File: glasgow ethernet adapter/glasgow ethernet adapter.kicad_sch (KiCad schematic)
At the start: 25 parts, among them J1 RJ45_Shielded, J2 Conn_02x10_Counter_Clockwise_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, J3 Conn_02x10_Counter_Clockwise_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, Y1 25MHz

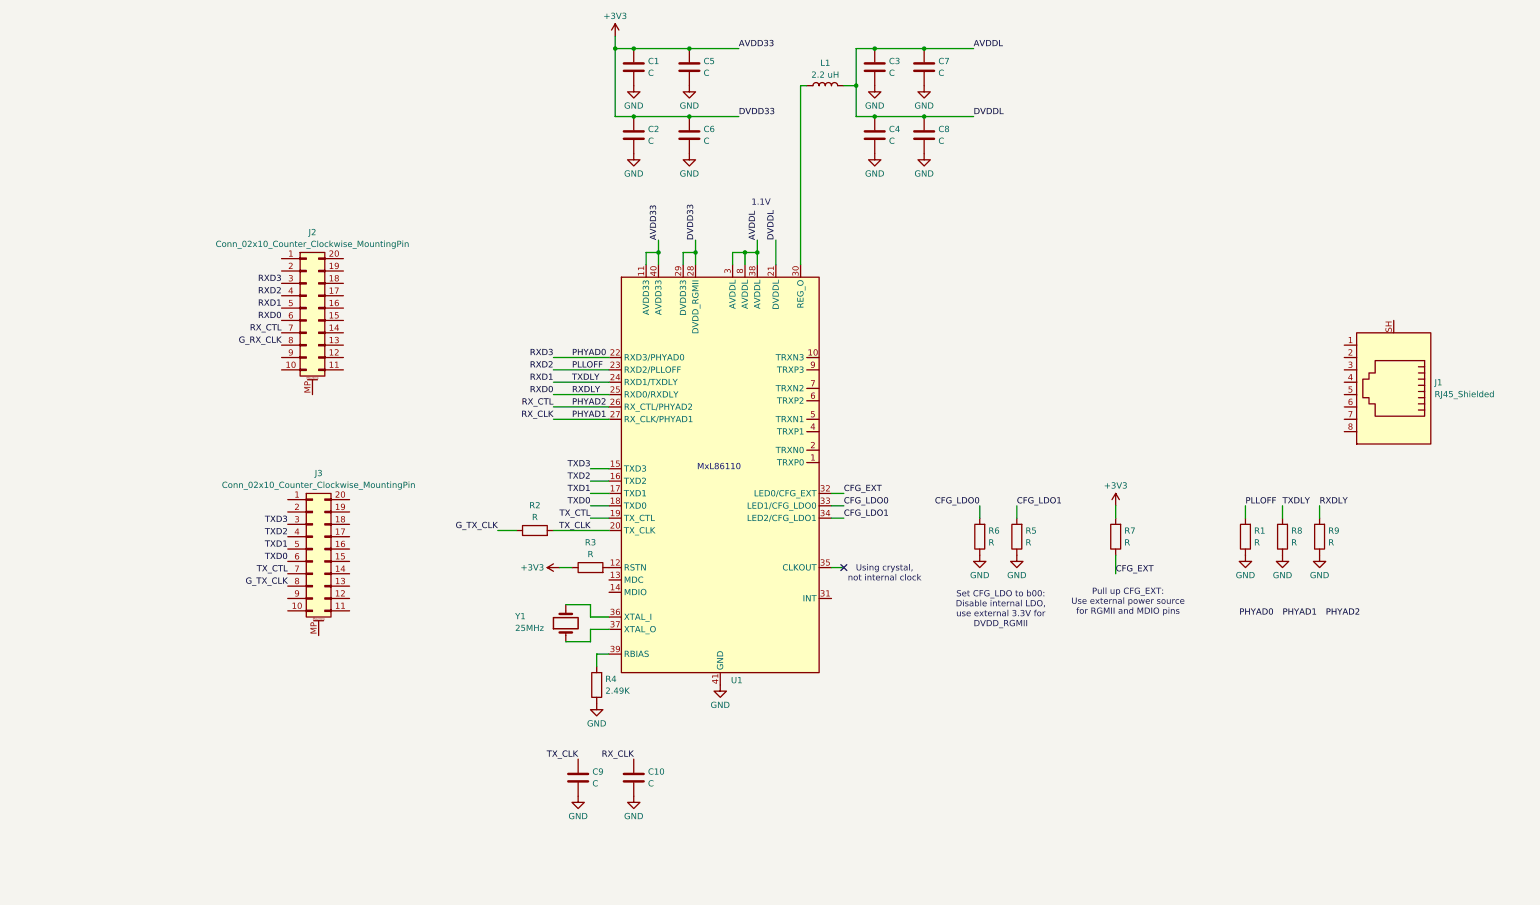
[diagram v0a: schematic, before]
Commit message: add transformer + protoype layout for transformer
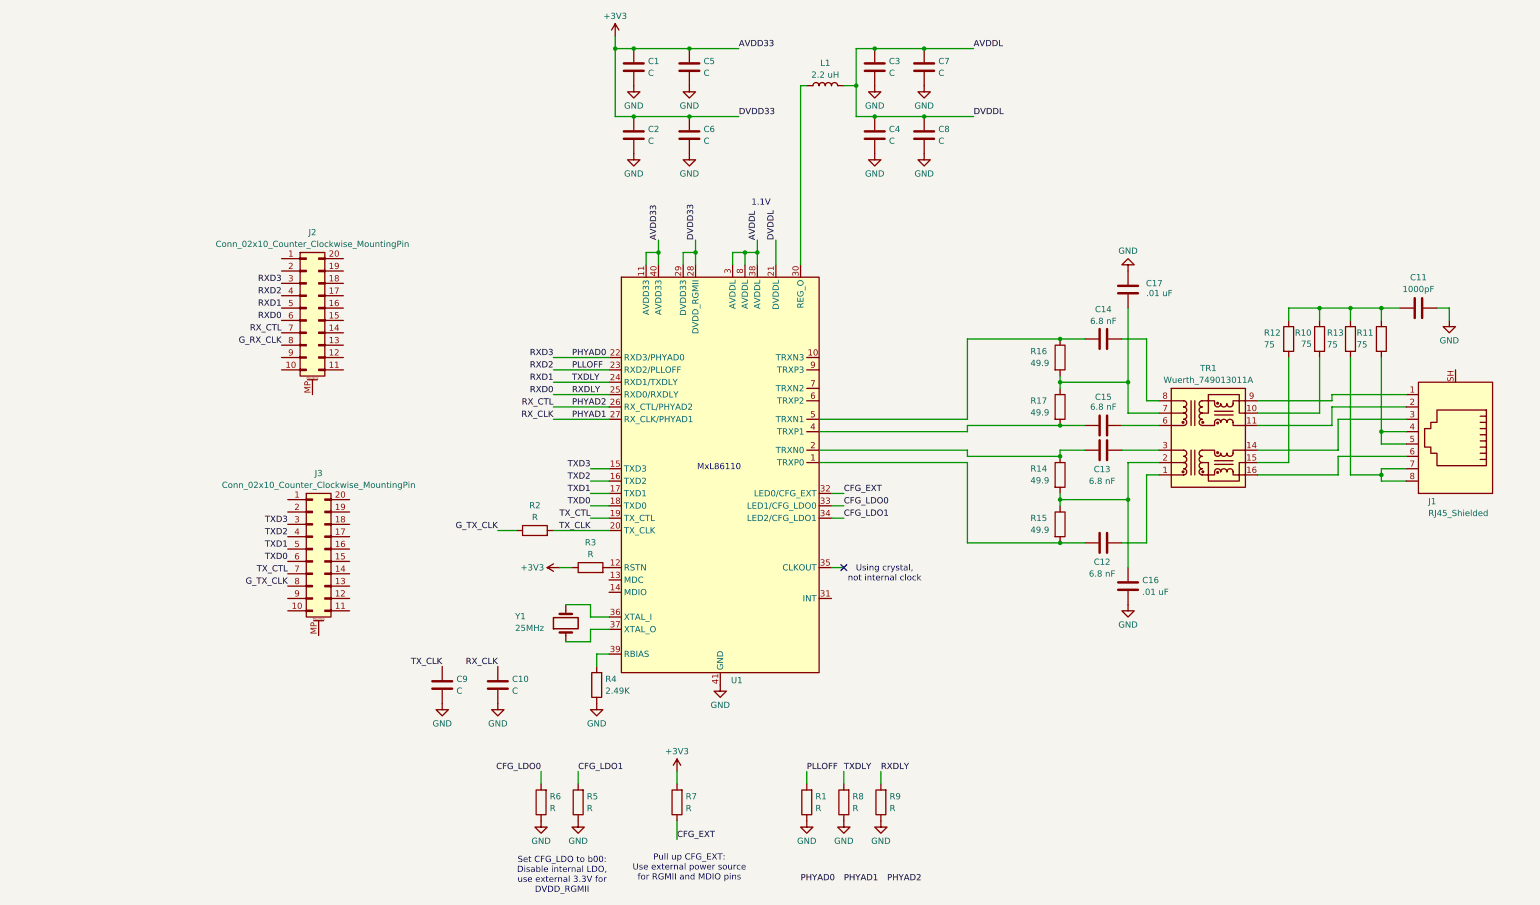
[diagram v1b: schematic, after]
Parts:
- added C11: 1000pF, symbol Device:C
- added C12, C13, C14, C15: 6.8 nF, symbol Device:C
- added C16, C17: .01 uF, symbol Device:C
- added R10, R11, R12, R13: 75, symbol Device:R
- added R14, R15, R16, R17: 49.9, symbol Device:R
- added TR1: Wuerth_749013011A, Transformer_SMD:Transformer_Ethernet_Wuerth_749013011A, symbol Transformer:Wuerth_749013011A
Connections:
- net GND: now also C11.1, C16.2, C17.2
- net at U1.1 (TRXP0): now also C12.2, R15.2
- net at U1.2 (TRXN0): now also C13.2, R14.1
- net at U1.4 (TRXP1): now also C15.2, R17.2
- net at U1.5 (TRXN1): now also C14.2, R16.1
- net at J1.1: now also TR1.9 (RX-)
- net at J1.2: now also TR1.11 (RX+)
- net at J1.3: now also TR1.14 (TX-)
- net at J1.4: now also J1.5, R11.2
- net at J1.6: now also TR1.16 (TX+)
- net at J1.7: now also J1.8, R13.2
- new net: C11.2, R10.1, R11.1, R12.1, R13.1
- new net: R10.2, TR1.10 (C_RX)
- new net: C16.1, R14.2, R15.1, TR1.2 (C_TD)
- new net: C17.1, R16.2, R17.1, TR1.7 (C_RD)
- new net: C15.1, TR1.6 (RD+)
- new net: C14.1, TR1.8 (RD-)
- new net: C13.1, TR1.3 (TD-)
- new net: R12.2, TR1.15 (C_TX)
- new net: C12.1, TR1.1 (TD+)
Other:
- moved on the sheet: C10, C9, J1, R1, R5, R6, R7, R8, R9

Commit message: WIP
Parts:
- removed C11: 1000pF, symbol Device:C
- removed J1: RJ45_Shielded, symbol Connector:RJ45_Shielded
- removed J2, J3: Conn_02x10_Counter_Clockwise_MountingPin, symbol Connector_Generic_MountingPin:Conn_02x10_Counter_Clockwise_MountingPin
- removed R10, R11, R12, R13: 75, symbol Device:R
- removed TR1: Wuerth_749013011A, Transformer_SMD:Transformer_Ethernet_Wuerth_749013011A, symbol Transformer:Wuerth_749013011A
- removed Y1: 25MHz, symbol Device:Crystal
- added J1: Glasgow Port, glasgow:Glasgow, symbol glasgow:Glasgow Ports
- added J2: RJ45_Amphenol_RJMG1BD3B8K1ANR, Connector_RJ:RJ45_Amphenol_RJMG1BD3B8K1ANR, symbol Connector:RJ45_Amphenol_RJMG1BD3B8K1ANR
- C1: renamed from C9; footprint (none) -> Capacitor_SMD:C_0603_1608Metric
- C10: renamed from C8; footprint (none) -> Capacitor_SMD:C_0603_1608Metric
- C11: renamed from C14; footprint (none) -> Capacitor_SMD:C_0603_1608Metric
- C12: renamed from C15; footprint (none) -> Capacitor_SMD:C_0603_1608Metric
- C13, C16, C5, C6: footprint (none) -> Capacitor_SMD:C_0603_1608Metric
- C14: renamed from C12; footprint (none) -> Capacitor_SMD:C_0603_1608Metric
- C15: renamed from C17; footprint (none) -> Capacitor_SMD:C_0603_1608Metric
- C2: renamed from C10; footprint (none) -> Capacitor_SMD:C_0603_1608Metric
- C3: renamed from C1; footprint (none) -> Capacitor_SMD:C_0603_1608Metric
- C4: renamed from C2; footprint (none) -> Capacitor_SMD:C_0603_1608Metric
- C7: renamed from C3; footprint (none) -> Capacitor_SMD:C_0603_1608Metric
- C8: renamed from C4; footprint (none) -> Capacitor_SMD:C_0603_1608Metric
- C9: renamed from C7; footprint (none) -> Capacitor_SMD:C_0603_1608Metric
- L1: footprint (none) -> Inductor_SMD:L_0603_1608Metric
- R1: renamed from R2; footprint (none) -> Resistor_SMD:R_0603_1608Metric
- R10: renamed from R16; footprint (none) -> Resistor_SMD:R_0603_1608Metric
- R11: renamed from R17; footprint (none) -> Resistor_SMD:R_0603_1608Metric
- R12: renamed from R14; footprint (none) -> Resistor_SMD:R_0603_1608Metric
- R13: renamed from R15; footprint (none) -> Resistor_SMD:R_0603_1608Metric
- R2: renamed from R6; footprint (none) -> Resistor_SMD:R_0603_1608Metric
- R3: renamed from R5; footprint (none) -> Resistor_SMD:R_0603_1608Metric
- R4: renamed from R3; footprint (none) -> Resistor_SMD:R_0603_1608Metric
- R5: renamed from R4; footprint (none) -> Resistor_SMD:R_0603_1608Metric
- R6: renamed from R7; footprint (none) -> Resistor_SMD:R_0603_1608Metric
- R7: renamed from R1; footprint (none) -> Resistor_SMD:R_0603_1608Metric
- R8, R9: footprint (none) -> Resistor_SMD:R_0603_1608Metric
- U1: value ~ -> MxL86110; footprint (none) -> Package_DFN_QFN:QFN-40-1EP_5x5mm_P0.4mm_EP3.8x3.8mm
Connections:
- net +3V3: now also R8.1, R9.1, J1.AV, J1.BV
- net GND: now also J1.A0G, J1.A1G, J1.A2G, J1.A3G, J1.A4G, J1.A5G, J1.A6G, J1.A7G, J1.AXG, J1.B0G, J1.B1G, J1.B2G, J1.B3G, J1.B4G, J1.B5G, J1.B6G, J1.B7G, J1.BXG, J2.R8; no longer R8.1, R9.1
- net G_RX_CLK: now also J1.A0
- net G_TX_CLK: now also J1.B0
- net PHYAD0: now also J1.A5
- net PHYAD2: now also J1.A1
- net PLLOFF: now also J1.A4
- net RXD0: now also J1.A2
- net RXD1: now also J1.A3
- net TXD0: now also J1.B2
- net TXD1: now also J1.B3
- net TXD2: now also J1.B4
- net TXD3: now also J1.B5
- net TX_CTL: now also J1.B1
- net at C16.1, R12.2, R13.1: now also J2.R5 (RCT)
- net MDIO: now reaches U1.14 (MDIO)
- net MDIO: now also J1.B6
- net MDINT: now reaches U1.31 (INT)
- net MDINT: now also J1.A7
- net GPC: now reaches U1.35 (CLKOUT)
- net GPC: now also J1.A6
- net at C15.1, R10.2, R11.1: now also J2.R4 (TCT)
- net at C12.1: now also J2.R2 (TD-)
- net at C11.1: now also J2.R1 (TD+)
- net at C13.1: now also J2.R3 (RD+)
- net at C14.1: now also J2.R6 (RD-)
- no-connect marks 1 -> 2
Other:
- note added: "Pull up RXDLY, TXDLY: 2ns delay by default"
- note removed: "Using crystal, not internal clock"
- moved on the sheet: R8, R9

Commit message: WIP
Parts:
- removed J2: RJ45_Amphenol_RJMG1BD3B8K1ANR, Connector_RJ:RJ45_Amphenol_RJMG1BD3B8K1ANR, symbol Connector:RJ45_Amphenol_RJMG1BD3B8K1ANR
- removed R1, R2, R3, R6, R7, R8, R9: R, Resistor_SMD:R_0603_1608Metric, symbol Device:R
- added C17, C20: 4.7u, Capacitor_SMD:C_1206_3216Metric, symbol Device:C
- added C18, C19, C21, C22: 0.1u, Capacitor_SMD:C_0402_1005Metric, symbol Device:C
- added D1, D2, D3: LED, Diode_SMD:D_0603_1608Metric, symbol Device:LED
- added J2: RJ45_Amphenol_RJMG1S8008101BR, glasgow:AMPHENOL_RJMG1S8008101BR, symbol glasgow:RJ45_Amphenol_RJMG1S8008101BR
- added R1, R2, R3, R4, R5, R6, R7, R8, R9: R-3-way, glasgow:R-3-Way_0402_1005Metric, symbol glasgow:R-3-way
- added R10: 0, Resistor_SMD:R_0402_1005Metric, symbol Device:R
- added R17, R18, R19: R, Resistor_SMD:R_0402_1005Metric, symbol Device:R
- C1, C2: value C -> 12p; footprint Capacitor_SMD:C_0603_1608Metric -> Capacitor_SMD:C_0402_1005Metric
- C10, C3, C4, C5, C6, C7, C8, C9: value C -> 0.1u; footprint Capacitor_SMD:C_0603_1608Metric -> Capacitor_SMD:C_0402_1005Metric
- R11: renamed from R4; footprint Resistor_SMD:R_0603_1608Metric -> Resistor_SMD:R_0402_1005Metric
- R12: renamed from R5; footprint Resistor_SMD:R_0603_1608Metric -> Resistor_SMD:R_0402_1005Metric
- R13: renamed from R10; footprint Resistor_SMD:R_0603_1608Metric -> Resistor_SMD:R_0402_1005Metric
- R14: renamed from R11; footprint Resistor_SMD:R_0603_1608Metric -> Resistor_SMD:R_0402_1005Metric
- R15: renamed from R12; footprint Resistor_SMD:R_0603_1608Metric -> Resistor_SMD:R_0402_1005Metric
- R16: renamed from R13; footprint Resistor_SMD:R_0603_1608Metric -> Resistor_SMD:R_0402_1005Metric
- U1: footprint Package_DFN_QFN:QFN-40-1EP_5x5mm_P0.4mm_EP3.8x3.8mm -> glasgow:QFN-40-1EP_5x5mm_P0.4mm_EP3.8x3.8mm
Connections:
- net G_RX_CLK is gone; now on net GPC: J1.A0
- net G_TX_CLK is gone; now on net TX_CLK: J1.B0
- net +3V3: now also C17.1, C18.1, C20.1, C21.1, R1.3, R2.1, R3.3, R4.1, R5.1, R6.3, R7.1, R8.1, R9.1
- net AVDDL: now also C19.1
- net CFG_EXT: now also R17.1, R9.2
- net CFG_LDO0: now also R18.1, R3.2
- net CFG_LDO1: now also R19.1, R6.2
- net GND: now also C17.2, C18.2, C19.2, C20.2, C21.2, C22.2, D1.1 (K), D2.1 (K), D3.1 (K), J2.8 (RD-), R1.1, R10.2, R2.3, R3.1, R4.3, R5.3, R6.1, R7.3, R8.3, R9.3
- net GPC: no longer J1.A6
- net MDINT: now also J1.A1; no longer J1.A7
- net PHYAD0: now also J1.A7, R2.2; no longer J1.A5
- net PHYAD1: now also J1.A2, R5.2
- net PHYAD2: now also J1.A3, R8.2; no longer J1.A1
- net PLLOFF: now also J1.A6, R1.2; no longer J1.A4
- net RXD0: now also J1.A4, R7.2; no longer J1.A2
- net RXD1: now also J1.A5, R4.2; no longer J1.A3
- net RX+: now reaches C13.2, R15.1
- net RX+: now also U1.6 (TRXP2); no longer U1.2 (TRXN0)
- net at C16.1, R15.2, R16.1: now also J2.6 (RCT)
- net RX-: now reaches C14.2, R16.2
- net RX-: now also U1.7 (TRXN2); no longer U1.1 (TRXP0)
- net +1V1: now reaches L1.1, U1.30 (REG_O)
- net TX-: now reaches C12.2, R14.2
- net TX-: now also U1.5 (TRXN1); no longer U1.4 (TRXP1)
- net TX+: now reaches C11.2, R13.1
- net TX+: now also U1.4 (TRXP1); no longer U1.5 (TRXN1)
- net at C15.1, R13.2, R14.1: now also J2.3 (TCT)
- net T-: now reaches C12.1
- net T-: now also J2.2 (TD-)
- net T+: now reaches C11.1
- net T+: now also J2.1 (TD+)
- net R+: now reaches C13.1
- net R+: now also J2.7 (RD+)
- net R-: now reaches C14.1
- net R-: now also J2.8 (RD-)
- new net: D1.2 (A), R17.2
- new net: D3.2 (A), R19.2
- new net: D2.2 (A), R18.2
- new net C_GND: C22.1, J2.SH, R10.1
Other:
- note added: "1% precision resistor for calibration"
- note added: "connector/chassis ground"
- moved on the sheet: C1, C10, C11, C12, C13, C14, C15, C16, C2, C3, C4, C5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

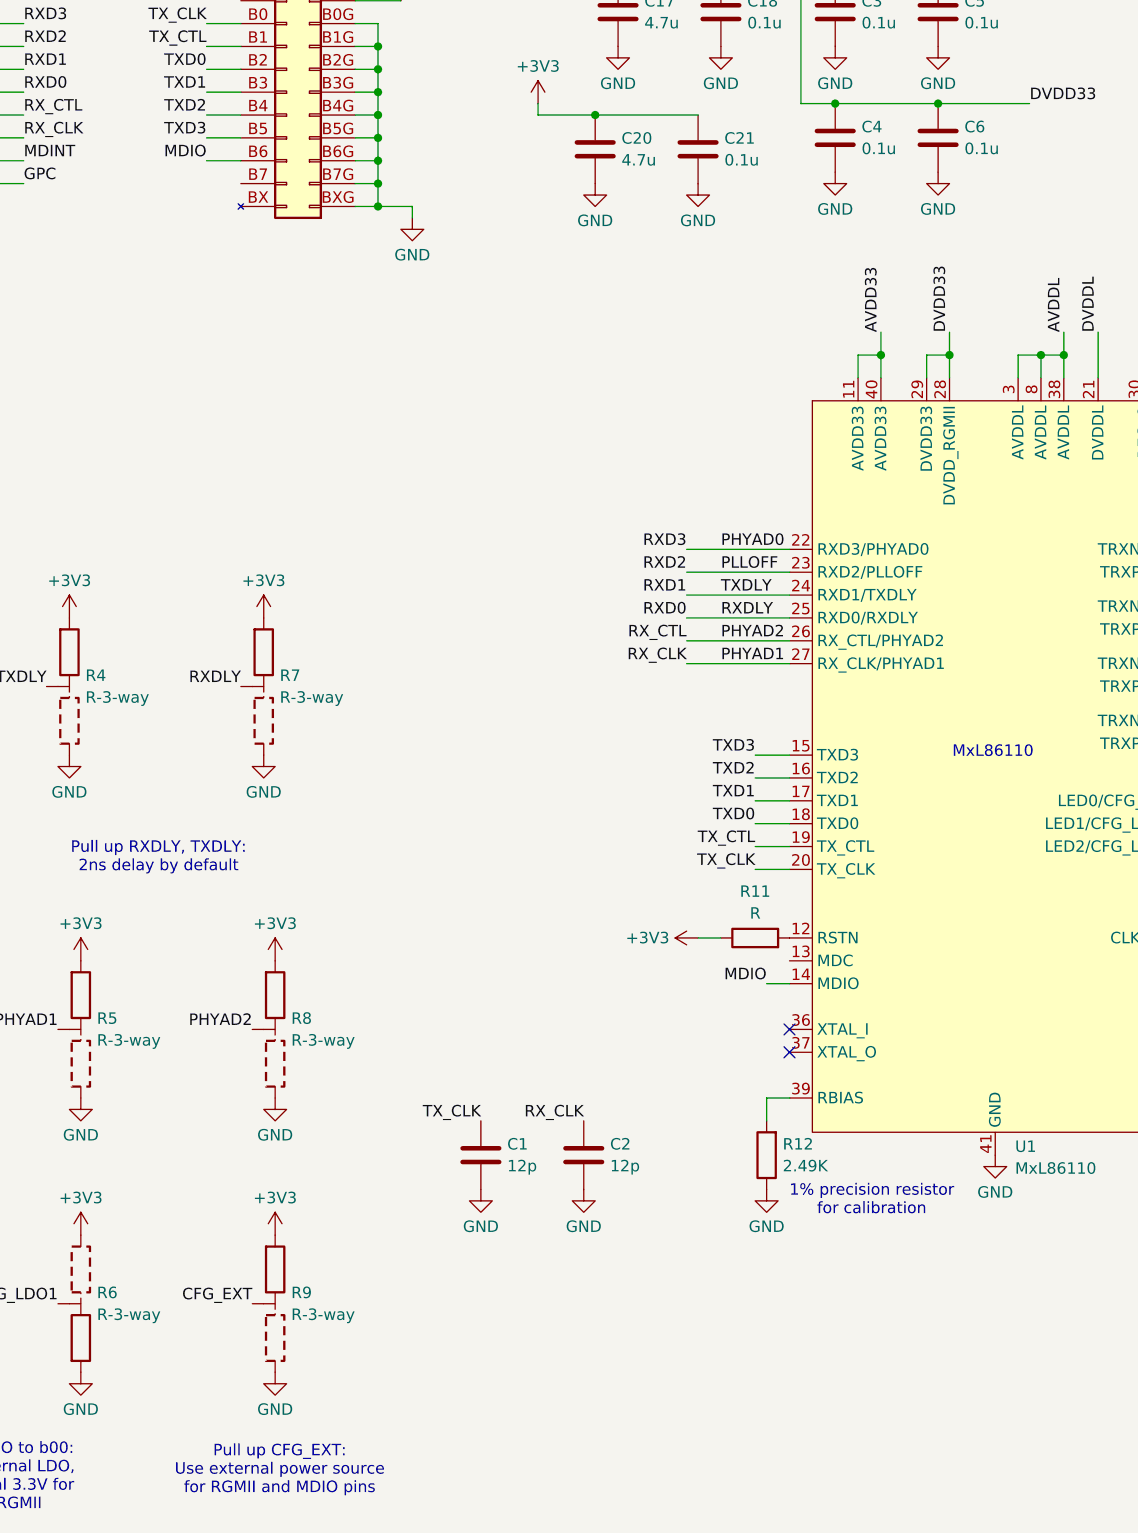
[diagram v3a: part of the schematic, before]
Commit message: wip - connect MDC, add crystal
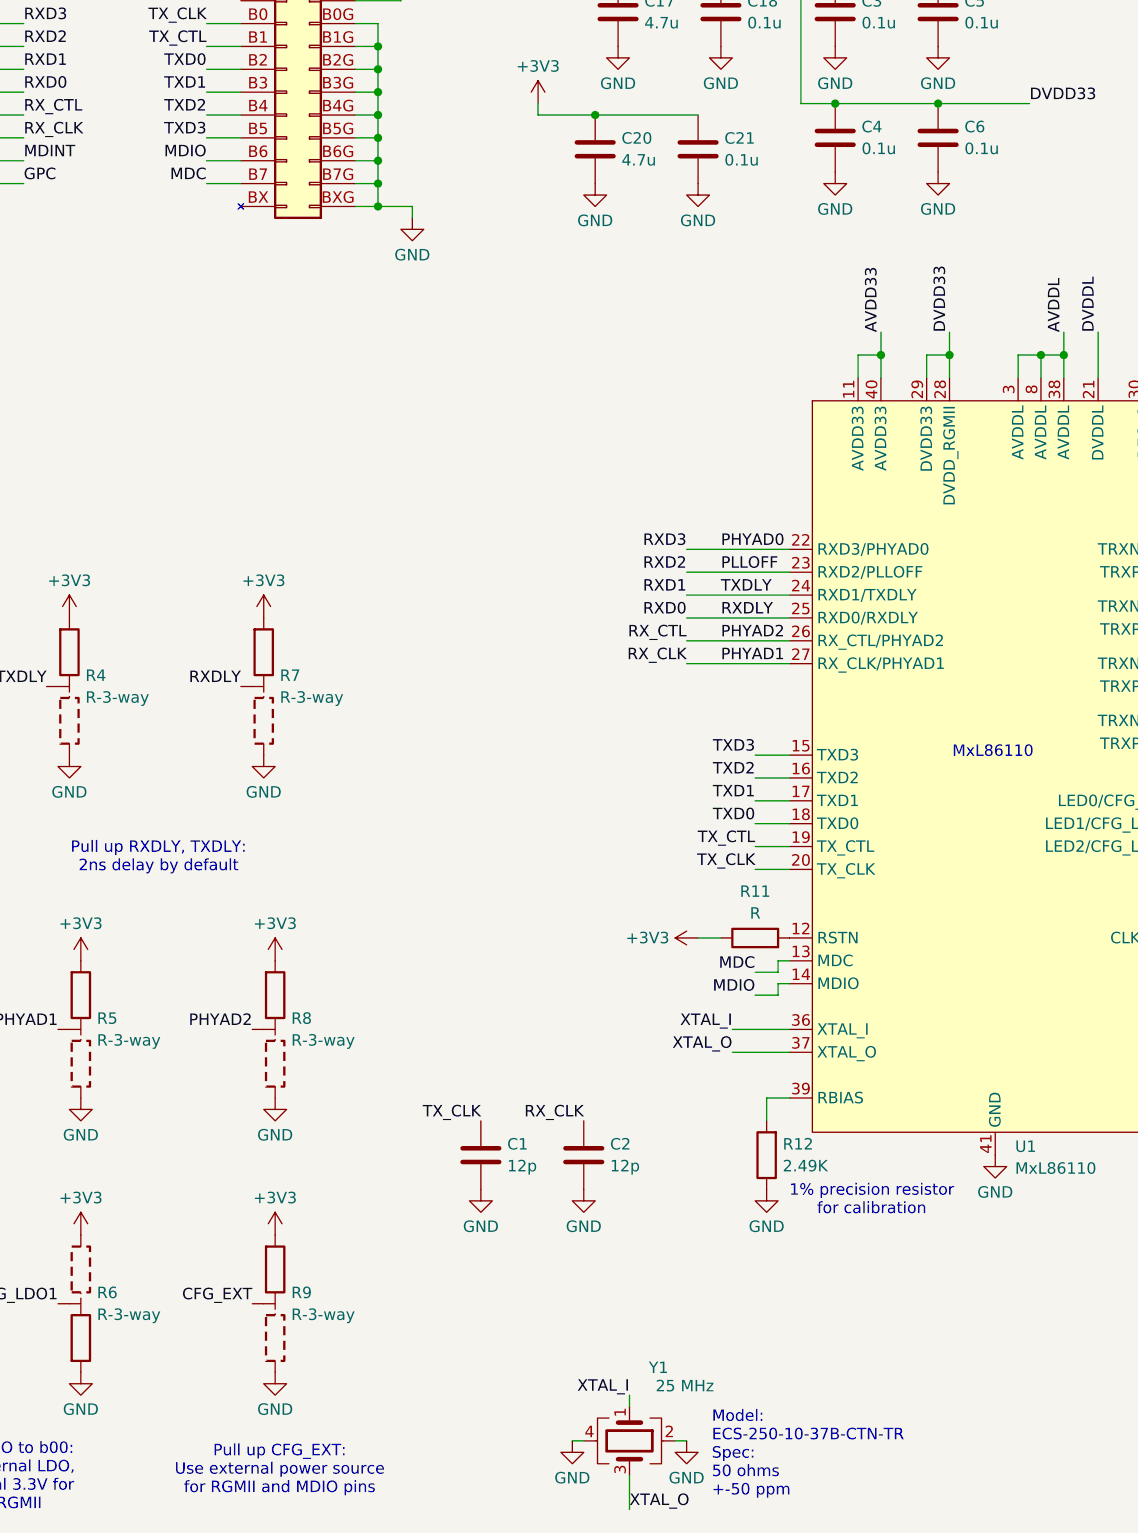
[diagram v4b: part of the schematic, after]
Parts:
- added Y1: 25 MHz, glasgow:XTAL_ECS-160-9-37-CKM-TR, symbol Device:Crystal_GND24
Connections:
- net GND: now also Y1.2, Y1.4
- net MDC: now reaches U1.13 (MDC)
- net MDC: now also J1.B7
- net XTAL_I: now reaches U1.36 (XTAL_I)
- net XTAL_I: now also Y1.1
- net XTAL_O: now reaches U1.37 (XTAL_O)
- net XTAL_O: now also Y1.3
- no-connect marks 2 -> 0
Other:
- note added: "Model: ECS-250-10-37B-CTN-TR Spec: 50 ohms +-50 ppm"
